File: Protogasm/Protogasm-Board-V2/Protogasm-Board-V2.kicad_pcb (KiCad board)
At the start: 2 copper layers, 68.6 x 53.3 mm, 10 parts, among them J1 Neopixel_Ring_Header, M1 Motor_DC, Q1 FQP30N06L, SW1 Rotary_Encoder_Switch, U1 Arduino_UNO_R3, U2 MPX5050GP

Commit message: Finalize protogasm board V2 (the basic remake)
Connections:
- net Net-(D1-Pad2) renamed /MOTOR-
- net Net-(J1-Pad2) renamed /D10
- net Net-(Q1-Pad1) renamed /D9
- net Net-(R2-Pad2) renamed /AREF
- net Net-(SW1-PadA) renamed /D2
- net Net-(SW1-PadB) renamed /D3
- net Net-(SW1-PadS2) renamed /D5
- net Net-(U1-Pad9) renamed /A0
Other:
- board text added: "Protogasm V2 Arduino UNO R3 Shield github.com/Edging-Machines sqrt10pi"

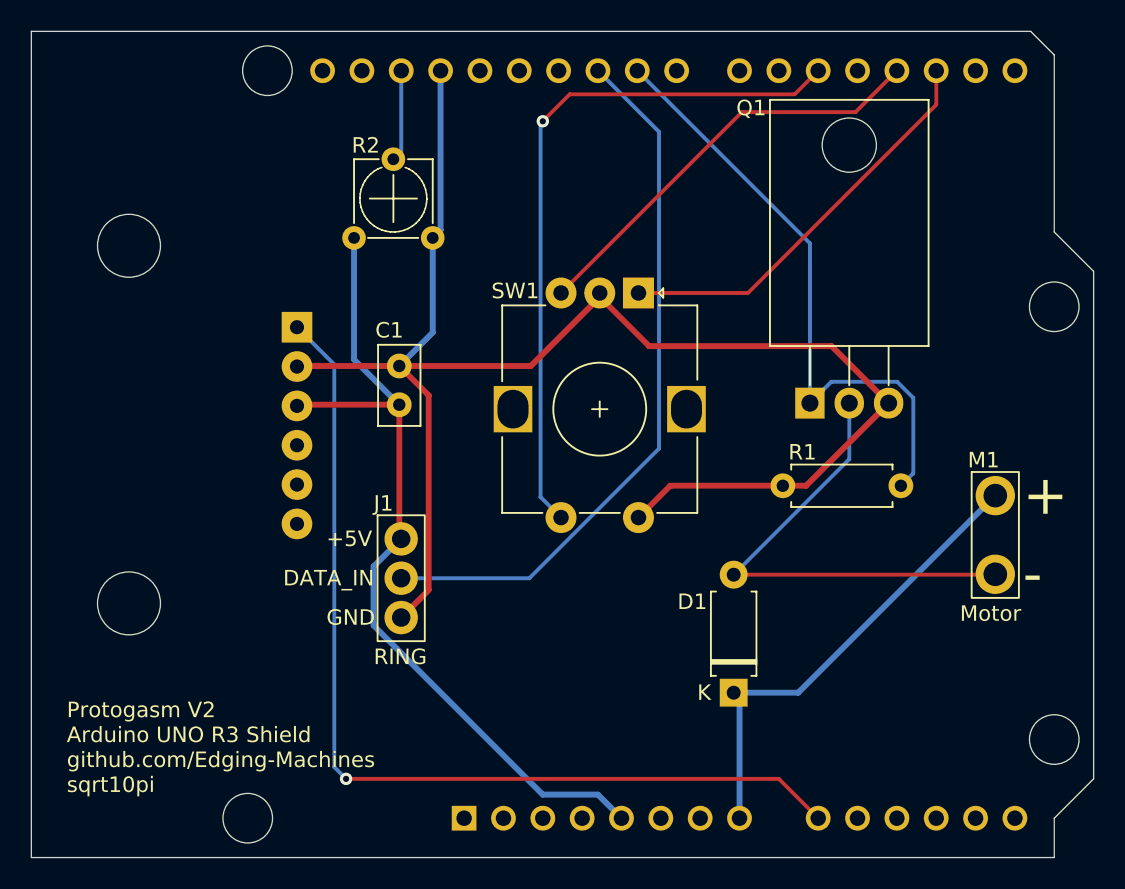
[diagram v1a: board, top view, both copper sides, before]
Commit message: Move SW1 to line up with case
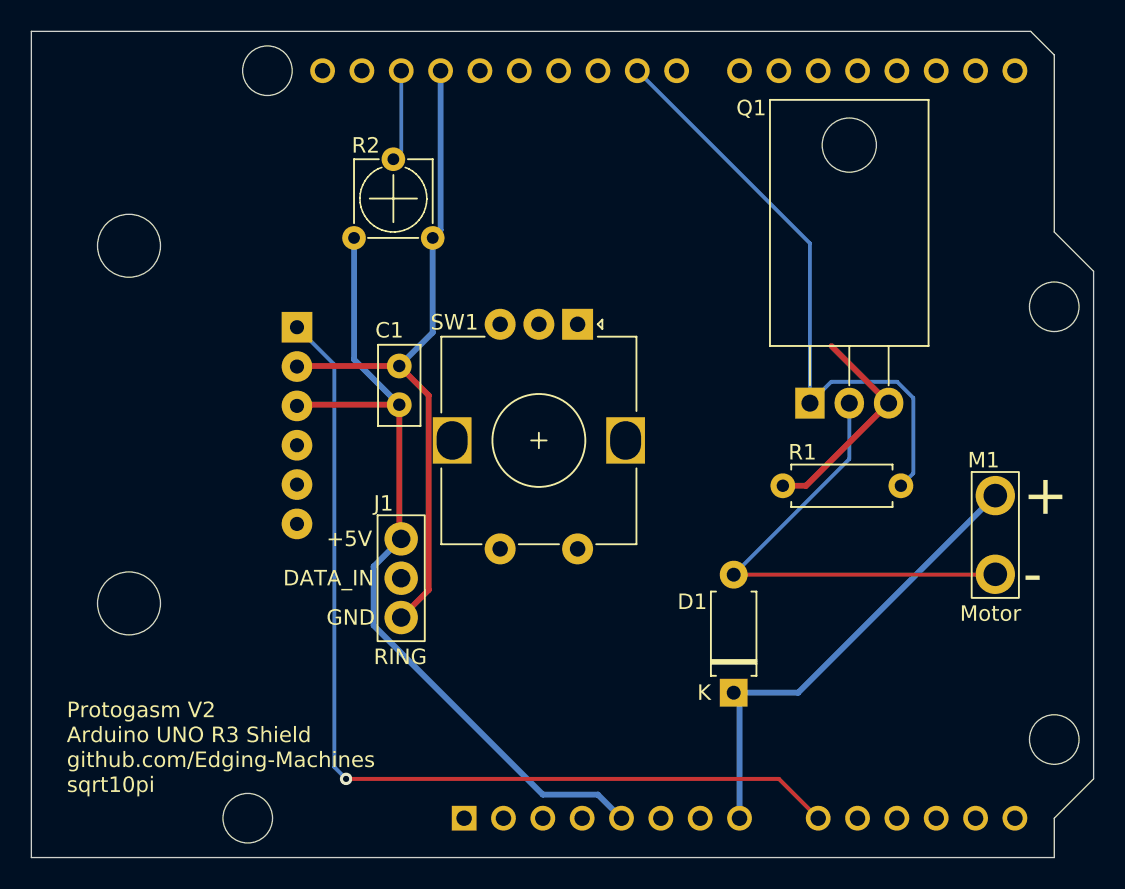
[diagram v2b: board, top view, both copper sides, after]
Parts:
- moved SW1 4.42 mm to (144.5, 90.0)
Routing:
- net /D10: track 46.1 -> 0.00 mm
- net /D5: track 45.4 -> 0.00 mm, vias 1 -> 0
- net GND: track 100.6 -> 58.8 mm
- net /D3: track 27.6 -> 0.00 mm
- net /D2: track 26.5 -> 0.00 mm
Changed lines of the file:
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@@
   )
   (footprint "Rotary_Encoder:RotaryEncoder_Alps_EC12E-Switch_Vertical_H20mm" (layer "F.Cu")
-    (at 148.4162 88.011 -90)
+    (at 144.486 90.032 -90)
     (descr "Alps rotary encoder, EC12E... with switch, vertical shaft, http://www.alps.com/prod/info/E/HTML/Encoder/Incremental/EC12E/EC12E1240405.html & http://cdn-reichelt.de/documents/datenblatt/F100/402097STEC12E08.PDF")
     (tags "rotary encoder")
@@
     (effects (font (size 1 1) (thickness 0.15)) (justify left))
   )
+  (target plus (at 177.8 124.46) (size 5) (width 0.05) (layer "Edge.Cuts"))
   (segment (start 132.973 95.2246) (end 132.973 103.763) (width 0.381) (layer "F.Cu") (net 1))
   (segment (start 132.973 103.763) (end 133.096 103.886) (width 0.381) (layer "F.Cu") (net 1))
@@
   (segment (start 130.052 92.3036) (end 130.052 84.455) (width 0.381) (layer "B.Cu") (net 1))
   (segment (start 132.973 92.7246) (end 126.4052 92.7246) (width 0.381) (layer "F.Cu") (net 2))
-  (segment (start 141.4634 92.7246) (end 132.973 92.7246) (width 0.381) (layer "F.Cu") (net 2))
-  (segment (start 145.9162 88.011) (end 145.9162 88.2718) (width 0.381) (layer "F.Cu") (net 2))
-  (segment (start 157.738 100.457) (end 150.4702 100.457) (width 0.381) (layer "F.Cu") (net 2))
-  (segment (start 145.9162 88.011) (end 145.9162 88.2582) (width 0.381) (layer "F.Cu") (net 2))
   (segment (start 134.874 94.6256) (end 134.874 107.188) (width 0.381) (layer "F.Cu") (net 2))
-  (segment (start 145.9162 88.2582) (end 149.098 91.44) (width 0.381) (layer "F.Cu") (net 2))
   (segment (start 164.5666 95.123) (end 159.2326 100.457) (width 0.381) (layer "F.Cu") (net 2))
   (segment (start 132.973 92.7246) (end 134.874 94.6256) (width 0.381) (layer "F.Cu") (net 2))
@@
   (segment (start 160.8836 91.44) (end 164.5666 95.123) (width 0.381) (layer "F.Cu") (net 2))
   (segment (start 159.2326 100.457) (end 157.738 100.457) (width 0.381) (layer "F.Cu") (net 2))
-  (segment (start 145.9162 88.2718) (end 141.4634 92.7246) (width 0.381) (layer "F.Cu") (net 2))
   (segment (start 134.874 107.188) (end 133.096 108.966) (width 0.381) (layer "F.Cu") (net 2))
-  (segment (start 150.4702 100.457) (end 148.4162 102.511) (width 0.381) (layer "F.Cu") (net 2))
-  (segment (start 149.098 91.44) (end 160.8836 91.44) (width 0.381) (layer "F.Cu") (net 2))
   (segment (start 135.64 83.947) (end 135.132 84.455) (width 0.381) (layer "B.Cu") (net 2))
   (segment (start 135.132 90.5656) (end 132.973 92.7246) (width 0.381) (layer "B.Cu") (net 2))
@@
   (segment (start 154.563 106.1974) (end 162.0266 98.7338) (width 0.25) (layer "B.Cu") (net 4))
   (segment (start 162.0266 98.7338) (end 162.0266 95.123) (width 0.25) (layer "B.Cu") (net 4))
-  (segment (start 141.374343 106.426) (end 149.740711 98.059632) (width 0.25) (layer "B.Cu") (net 5))
-  (segment (start 149.740711 77.600711) (end 145.8 73.66) (width 0.25) (layer "B.Cu") (net 5))
-  (segment (start 149.740711 98.059632) (end 149.740711 77.600711) (width 0.25) (layer "B.Cu") (net 5))
-  (segment (start 133.096 106.426) (end 141.374343 106.426) (width 0.25) (layer "B.Cu") (net 5))
   (segment (start 165.358 100.457) (end 166.157999 99.657001) (width 0.25) (layer "B.Cu") (net 6))
   (segment (start 159.4866 84.8066) (end 148.34 73.66) (width 0.25) (layer "B.Cu") (net 6))
@@
   (segment (start 133.1 78.867) (end 132.592 79.375) (width 0.25) (layer "B.Cu") (net 7))
   (segment (start 133.1 73.66) (end 133.1 78.867) (width 0.25) (layer "B.Cu") (net 7))
-  (segment (start 155.483127 88.011) (end 148.4162 88.011) (width 0.25) (layer "F.Cu") (net 8))
-  (segment (start 167.64 75.854127) (end 155.483127 88.011) (width 0.25) (layer "F.Cu") (net 8))
-  (segment (start 167.64 73.66) (end 167.64 75.854127) (width 0.25) (layer "F.Cu") (net 8))
-  (segment (start 162.421521 76.338479) (end 165.1 73.66) (width 0.25) (layer "F.Cu") (net 9))
-  (segment (start 155.088721 76.338479) (end 162.421521 76.338479) (width 0.25) (layer "F.Cu") (net 9))
-  (segment (start 143.4162 88.011) (end 155.088721 76.338479) (width 0.25) (layer "F.Cu") (net 9))
-  (segment (start 142.24 76.924511) (end 143.980511 75.184) (width 0.25) (layer "F.Cu") (net 10))
-  (segment (start 143.980511 75.184) (end 158.496 75.184) (width 0.25) (layer "F.Cu") (net 10))
-  (segment (start 158.496 75.184) (end 160.02 73.66) (width 0.25) (layer "F.Cu") (net 10))
-  (via (at 142.24 76.924511) (size 0.8) (drill 0.4) (layers "F.Cu" "B.Cu") (net 10))
-  (segment (start 142.24 76.924511) (end 142.091689 76.924511) (width 0.25) (layer "B.Cu") (net 10))
-  (segment (start 143.4162 102.511) (end 142.091689 101.186489) (width 0.25) (layer "B.Cu") (net 10))
-  (segment (start 142.091689 101.186489) (end 142.091689 76.924511) (width 0.25) (layer "B.Cu") (net 10))
   (segment (start 157.48 119.38) (end 160.02 121.92) (width 0.25) (layer "F.Cu") (net 23))
   (segment (start 129.54 119.38) (end 157.48 119.38) (width 0.25) (layer "F.Cu") (net 23))

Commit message: Move components so that SW1 and MPX5050GP will fit
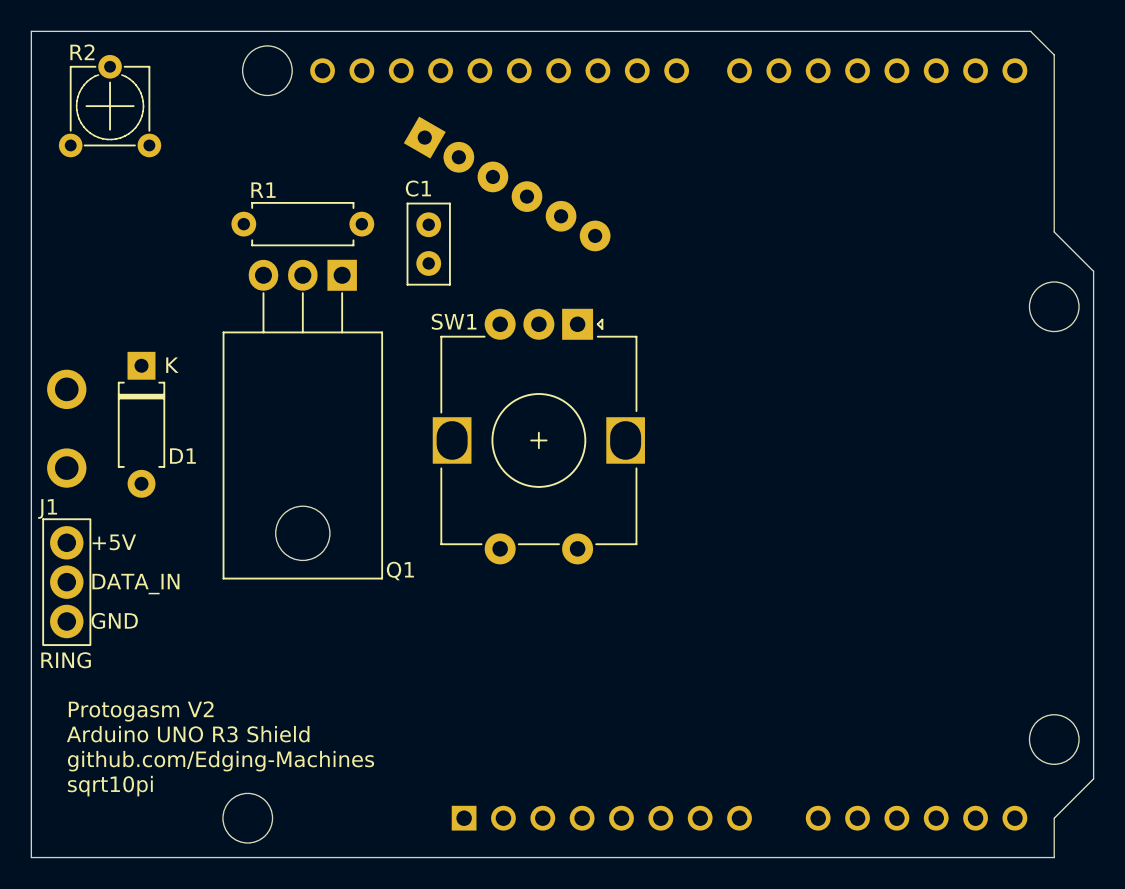
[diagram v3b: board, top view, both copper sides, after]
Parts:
- M1: moved to B.Cu
- moved M1 60.3 mm to (111.5, 94.2), turned to 180 degrees
- moved D1 43.7 mm to (116.3, 92.7), turned to -90 degrees
- moved R1 38.7 mm to (130.6, 83.6)
- moved Q1 31.3 mm to (129.3, 86.9), turned to 180 degrees
- moved J1 21.6 mm to (111.5, 104.1)
- moved R2 19.2 mm to (111.8, 78.5)
- moved U2 14.8 mm to (134.6, 78.0), turned to -120 degrees
- moved C1 9.31 mm to (134.9, 86.1)
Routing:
- net /A0: track 62.0 -> 0.00 mm, vias 1 -> 0
- net GND: track 58.8 -> 0.00 mm
- net +5V: track 54.8 -> 0.00 mm
- net /D9: track 39.8 -> 0.00 mm
- net /MOTOR-: track 31.1 -> 0.00 mm
- net +12V: track 30.4 -> 0.00 mm
- net /AREF: track 5.93 -> 0.00 mm
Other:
- board text added: "crystal back side low clearance"
- board text added: "tall"
- board text added: "tall Arduino components no footprints on back side"
- board text added: "tall components no footprints on back side"
